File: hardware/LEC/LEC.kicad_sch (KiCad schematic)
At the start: 25 parts, among them J1 54-00278, J10 Conn_01x02_Socket, J11 Conn_01x02_Socket, J12 Conn_01x02_Socket, J13 Conn_01x02_Socket, J14 Conn_01x02_Socket, J15 Conn_01x02_Socket, J16 Conn_01x02_Socket, J17 Conn_01x03_Socket, J18 Conn_01x03_Socket, J19 Conn_01x03_Socket, J2 54-00278, J3 54-00278, J4 54-00278, J5 54-00278, J6 54-00278, J7 54-00278, J8 54-00278, J9 Conn_01x02_Socket, U1 Pico, U2 ZETA-433-SO, U3 ADS1243, U4 W25Q128JVSIQ

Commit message: Added LPFs and updated power circuits. Tidied up a bit
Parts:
- removed AE1: Antenna, symbol Device:Antenna
- removed J10, J11, J12, J13, J14, J15, J16, J9: Conn_01x02_Socket, symbol Connector:Conn_01x02_Socket
- removed J17, J18, J19: Conn_01x03_Socket, symbol Connector:Conn_01x03_Socket
- removed R1: 10K, symbol Device:R
- removed U2: ZETA-433-SO, symbol RF_AM_FM:ZETA-433-SO
- removed U3: ADS1243, Package_SO:TSSOP-20_4.4x6.5mm_P0.65mm, symbol Analog_ADC:ADS1243
- removed U4: W25Q128JVSIQ, SOIC_128JVSIQ_WIN, symbol W25q128JVSIQ:W25Q128JVSIQ
- added C1 (x2): 100n, Capacitor_SMD:C_1206_3216Metric, symbol Device:C
- added C14: 10u, symbol Device:C
- added D1: 1N5817, Diode_THT:D_DO-41_SOD81_P10.16mm_Horizontal, symbol Diode:1N5817
- added J10, J9: Conn_01x02, symbol Connector_Generic:Conn_01x02
- added J11, J12, J13, J9: 54-00278, TENSILITY_54-00278, symbol 4_Pin_M8_Socket_Female:54-00278
- added U15: MCP3564RT-E/ST, TSSOP20_ST_MCH, symbol MCP3564:MCP3564RT-E_ST
- added U2: LM2940CT-5.0/NOPB, T03B, symbol LM2940CT_5_0_NOPB:LM2940CT-5.0_NOPB
- added U3: MC7809CTG, TO-220AB_ONS, symbol MC7809CTG:MC7809CTG
- added U4: W25Q128JVSIQ, SOIC_128JVSIQ_WIN, symbol W25Q128JVSIQ:W25Q128JVSIQ
- added U5, U6: MAX31855KASA, Package_SO:SOIC-8_3.9x4.9mm_P1.27mm, symbol Sensor_Temperature:MAX31855KASA
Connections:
- net +12V: now also J10.1 (Pin_1), J11.3, J12.3, U2.1 (IN)
- net +3.3V: now also C1.1, C1.1, U5.4 (V_CC), U6.4 (V_CC)
- net GND: now also J10.2 (Pin_2), J11.2, J12.2
- net at J8.1: now also U6.3 (T+)
- net at J8.2: now also U6.2 (T-)
- net at U1.1 (GPIO0): now also J13.1
- net GPIO7: now reaches U1.10 (GPIO7)
- net GPIO7: now also U15.15 (SDI)
- net GPIO8: now reaches U1.11 (GPIO8)
- net GPIO8: now also U6.7 (SO)
- net GPIO9: now reaches U1.12 (GPIO9)
- net GPIO9: now also U6.6 (~{CS})
- net GNDD: now reaches U1.13 (GND)
- net GNDD: now also U1.18 (GND), U1.23 (GND), U1.28 (GND), U1.3 (GND), U1.38 (GND), U1.8 (GND), U15.19 (DGND), U2.2 (GND), U4.4 (GND)
- net GPIO10: now reaches U1.14 (GPIO10)
- net GPIO10: now also U6.5 (SCK)
- net GPIO12: now reaches U1.16 (GPIO12)
- net GPIO12: now also U5.7 (SO)
- net GPIO13: now reaches U1.17 (GPIO13)
- net GPIO13: now also U5.6 (~{CS})
- net GPIO14: now reaches U1.19 (GPIO14)
- net GPIO14: now also U5.5 (SCK)
- net at U1.2 (GPIO1): now also J13.2
- net GPIO16: now reaches U1.21 (GPIO16)
- net GPIO16: now also U4.2 (DO_(IO1))
- net GPIO17: now reaches U1.22 (GPIO17)
- net GPIO17: now also U4.1 (/CS)
- net GPIO18: now reaches U1.24 (GPIO18)
- net GPIO18: now also U4.6 (CLK)
- net GPIO19: now reaches U1.25 (GPIO19)
- net GPIO19: now also U4.5 (DI_(IO0))
- net at U1.27 (GPIO21): now also J12.1
- net at U1.29 (GPIO22): now also J11.1
- net ADC_Power_Circuit/SHDN: now reaches U1.31 (GPIO26_ADC0)
- net GNDA: now reaches U1.33 (AGND)
- net GNDA: now also J1.2, J2.2, J3.2, J4.2, J5.2, J6.2, J7.2, C1.2, C1.2, C14.1, J9.2 (Pin_2), U15.2 (AGND), U15.3 (REFIN-), U3.2 (GROUND), U5.1 (GND), U6.1 (GND)
- net at U1.36 (3V3): now also U4.8 (VCC)
- net at U1.39 (VSYS): now also D1.1 (K)
- net at U1.4 (GPIO2): now also J13.3
- net at U1.5 (GPIO3): now also J13.4
- net GPIO4: now reaches U1.6 (GPIO4)
- net GPIO4: now also U15.16 (SDO)
- net GPIO5: now reaches U1.7 (GPIO5)
- net GPIO5: now also U15.13 (*CS)
- net GPIO6: now reaches U1.9 (GPIO6)
- net GPIO6: now also U15.14 (SCK)
- net lowPassFilter2/V_{in}: now reaches J3.1
- net at J3.3: now also J1.3, J2.3, J4.3, J5.3, J6.3, J7.3, U3.3 (OUTPUT)
- net lowPassFilter4/V_{in}: now reaches J5.1
- net lowPassFilter6/V_{in}: now reaches J7.1
- net lowPassFilter/V_{in}: now reaches J1.1
- net lowPassFilter3/V_{in}: now reaches J4.1
- net lowPassFilter5/V_{in}: now reaches J6.1
- net lowPassFilter1/V_{in}: now reaches J2.1
- new net: D1.2 (A), U2.3 (OUT)
- new net: J9.1, U5.3 (T+)
- new net: J9.2, U5.2 (T-)
- new net ADC_Power_Circuit/AVDDOUT: U15.1 (AVDD)
- new net ADC_Power_Circuit/DVDDOUT: U15.20 (DVDD)
- new net ADC_Power_Circuit/REFIN+/OUT: C14.2, U15.4 (REFIN+/OUT)
- new net ADC_Power_Circuit/VIN: J9.1 (Pin_1), U3.1 (INPUT)
- new net lowPassFilter/V_{out}: U15.5 (CH0)
- new net lowPassFilter1/V_{out}: U15.6 (CH1)
- new net lowPassFilter2/V_{out}: U15.7 (CH2)
- new net lowPassFilter3/V_{out}: U15.8 (CH3)
- new net lowPassFilter4/V_{out}: U15.9 (CH4)
- new net lowPassFilter5/V_{out}: U15.10 (CH5)
- new net lowPassFilter6/V_{out}: U15.11 (CH6)
- no-connect marks 10 -> 29
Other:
- added sheet ADC_Power_Circuit (ADC_Power_Circuit.kicad_sch)
- added sheet lowPassFilter (lowPassFilter.kicad_sch)
- added sheet lowPassFilter1 (untitled.kicad_sch)
- added sheet lowPassFilter2 (untitled.kicad_sch)
- added sheet lowPassFilter3 (untitled.kicad_sch)
- added sheet lowPassFilter4 (untitled.kicad_sch)
- added sheet lowPassFilter5 (untitled.kicad_sch)
- added sheet lowPassFilter6 (untitled.kicad_sch)
- note added: "Pressure Transducer Connectors"
- note added: "RF Module SPI Connector"
- note added: "Sensor Power Connector (3S LiPo Battery, 11.1V)"
- note added: "Servomotor Power Connector (2S LiPo Battery, 7.4V)"
- note added: "Servomotor connectors"
- note added: "Thermocouple Connectors"
- moved on the sheet: J1, U1

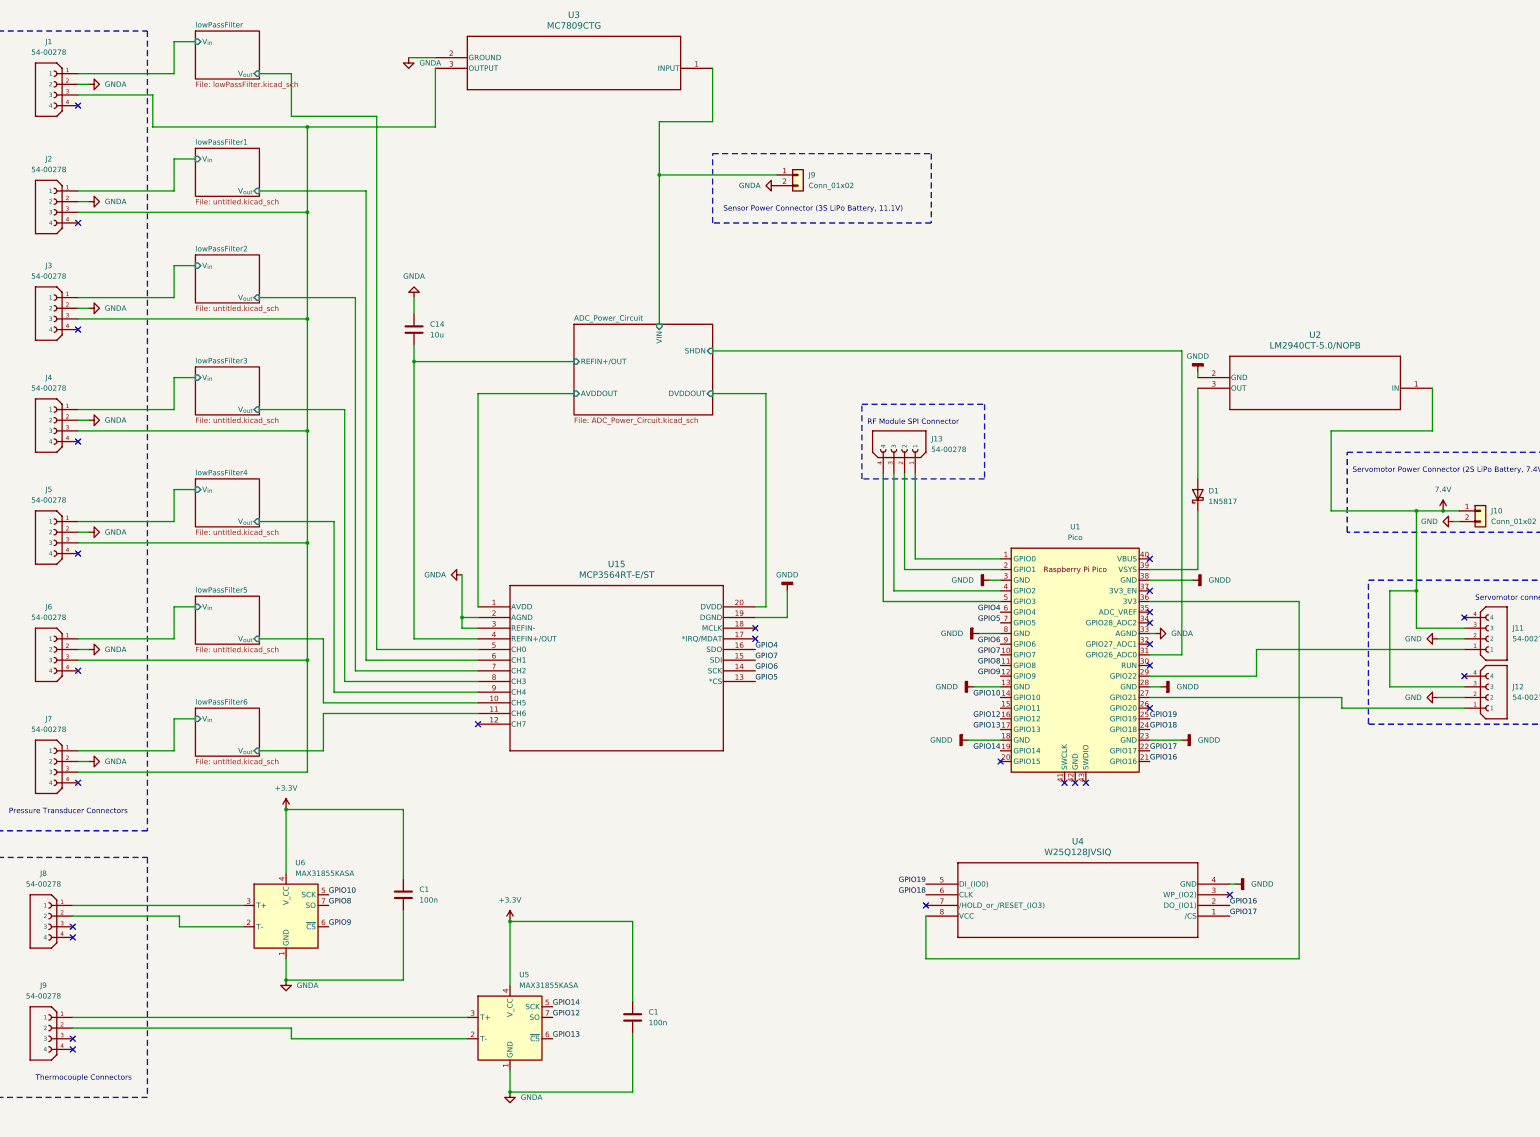
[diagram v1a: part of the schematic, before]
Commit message: Updated LVR selection and other optimizations. Need to update footprints and symbols
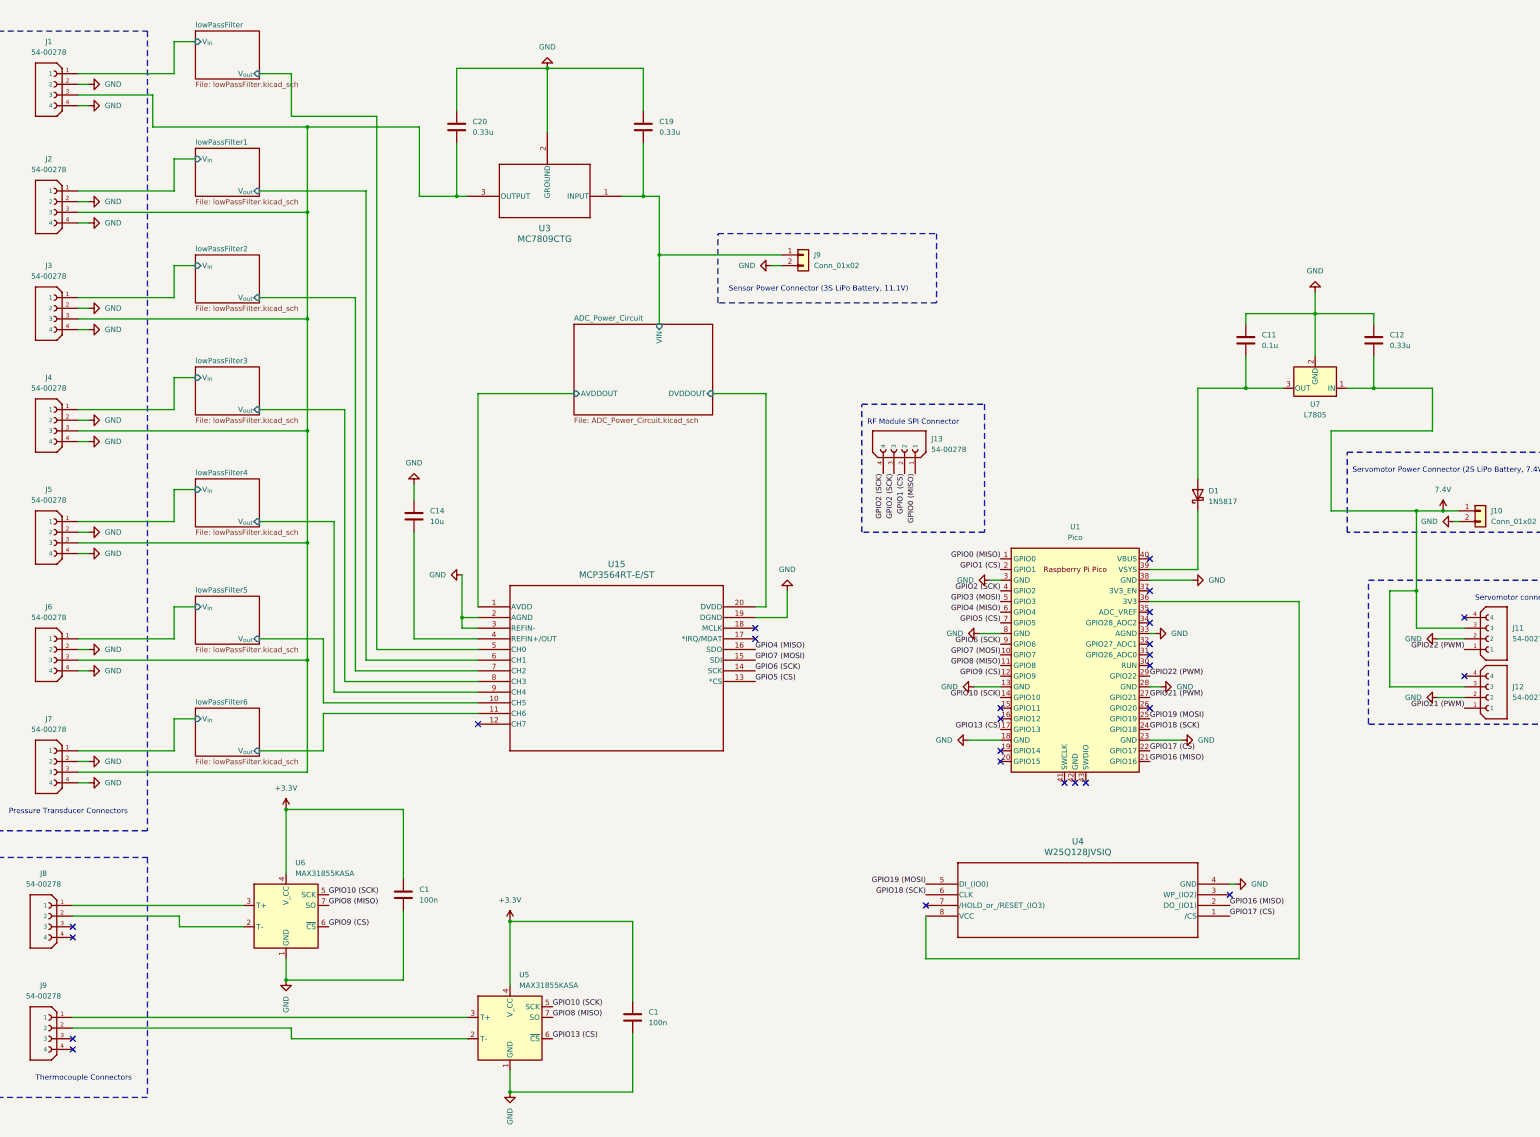
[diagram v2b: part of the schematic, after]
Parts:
- removed U2: LM2940CT-5.0/NOPB, T03B, symbol LM2940CT_5_0_NOPB:LM2940CT-5.0_NOPB
- added C11: 0.1u, symbol Device:C
- added C12, C19, C20: 0.33u, symbol Device:C
- added U7: L7805, symbol Regulator_Linear:L7805
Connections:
- net GNDA is gone; now on net GND: C1.2, C1.2, C14.1, J1.2, J2.2, J3.2, J4.2, J5.2, J6.2, J7.2, J9.2 (Pin_2), U1.33 (AGND), U15.2 (AGND), U15.3 (REFIN-), U3.2 (GROUND), U5.1 (GND), U6.1 (GND)
- net GNDD is gone; now on net GND: U1.13 (GND), U1.18 (GND), U1.23 (GND), U1.28 (GND), U1.3 (GND), U1.38 (GND), U1.8 (GND), U15.19 (DGND), U4.4 (GND)
- net +12V: now also C12.2, U7.1 (IN)
- net ADC_Power_Circuit/VIN: now also C19.2
- net GND: now also J1.4, J2.4, J3.4, J4.4, J5.4, J6.4, J7.4, C11.1, C12.1, C19.1, C20.1, U7.2 (GND)
- net at J1.3, J2.3, J3.3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: now also C20.2
- net GPIO0 (MISO): now reaches J13.1, U1.1 (GPIO0)
- net GPIO1 (CS): now reaches J13.2, U1.2 (GPIO1)
- net GPIO21 (PWM): now reaches J12.1, U1.27 (GPIO21)
- net GPIO22 (PWM): now reaches J11.1, U1.29 (GPIO22)
- net GPIO2 (SCK): now reaches J13.3, U1.4 (GPIO2)
- net GPIO2 (SCK): now also J13.4
- net GPIO3 (MOSI): now reaches U1.5 (GPIO3)
- net GPIO3 (MOSI): no longer J13.4
- net at D1.2 (A): now also C11.2, U7.3 (OUT)
- net ADC_Power_Circuit/REFIN+/OUT: no longer names the net of C14.2, U15.4 (REFIN+/OUT)
- net ADC_Power_Circuit/SHDN: no longer names the net of U1.31 (GPIO26_ADC0)
- net GPIO10 renamed GPIO10 (SCK)
- net GPIO10 (SCK): now also U5.5 (SCK)
- net GPIO12: no longer names the net of U1.16 (GPIO12)
- net GPIO12: no longer U5.7 (SO)
- net GPIO13 renamed GPIO13 (CS)
- net GPIO14: no longer names the net of U1.19 (GPIO14)
- net GPIO14: no longer U5.5 (SCK)
- net GPIO16 renamed GPIO16 (MISO)
- net GPIO17 renamed GPIO17 (CS)
- net GPIO18 renamed GPIO18 (SCK)
- net GPIO19 renamed GPIO19 (MOSI)
- net GPIO4 renamed GPIO4 (MISO)
- net GPIO5 renamed GPIO5 (CS)
- net GPIO6 renamed GPIO6 (SCK)
- net GPIO7 renamed GPIO7 (MOSI)
- net GPIO8 renamed GPIO8 (MISO)
- net GPIO8 (MISO): now also U5.7 (SO)
- net GPIO9 renamed GPIO9 (CS)
- no-connect marks 29 -> 26
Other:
- sheet ADC_Power_Circuit ports: added none; removed REFIN+/OUT, SHDN
- sheet lowPassFilter1: file untitled.kicad_sch -> lowPassFilter.kicad_sch
- sheet lowPassFilter2: file untitled.kicad_sch -> lowPassFilter.kicad_sch
- sheet lowPassFilter3: file untitled.kicad_sch -> lowPassFilter.kicad_sch
- sheet lowPassFilter4: file untitled.kicad_sch -> lowPassFilter.kicad_sch
- sheet lowPassFilter5: file untitled.kicad_sch -> lowPassFilter.kicad_sch
- sheet lowPassFilter6: file untitled.kicad_sch -> lowPassFilter.kicad_sch
- moved on the sheet: C14, J9, U3

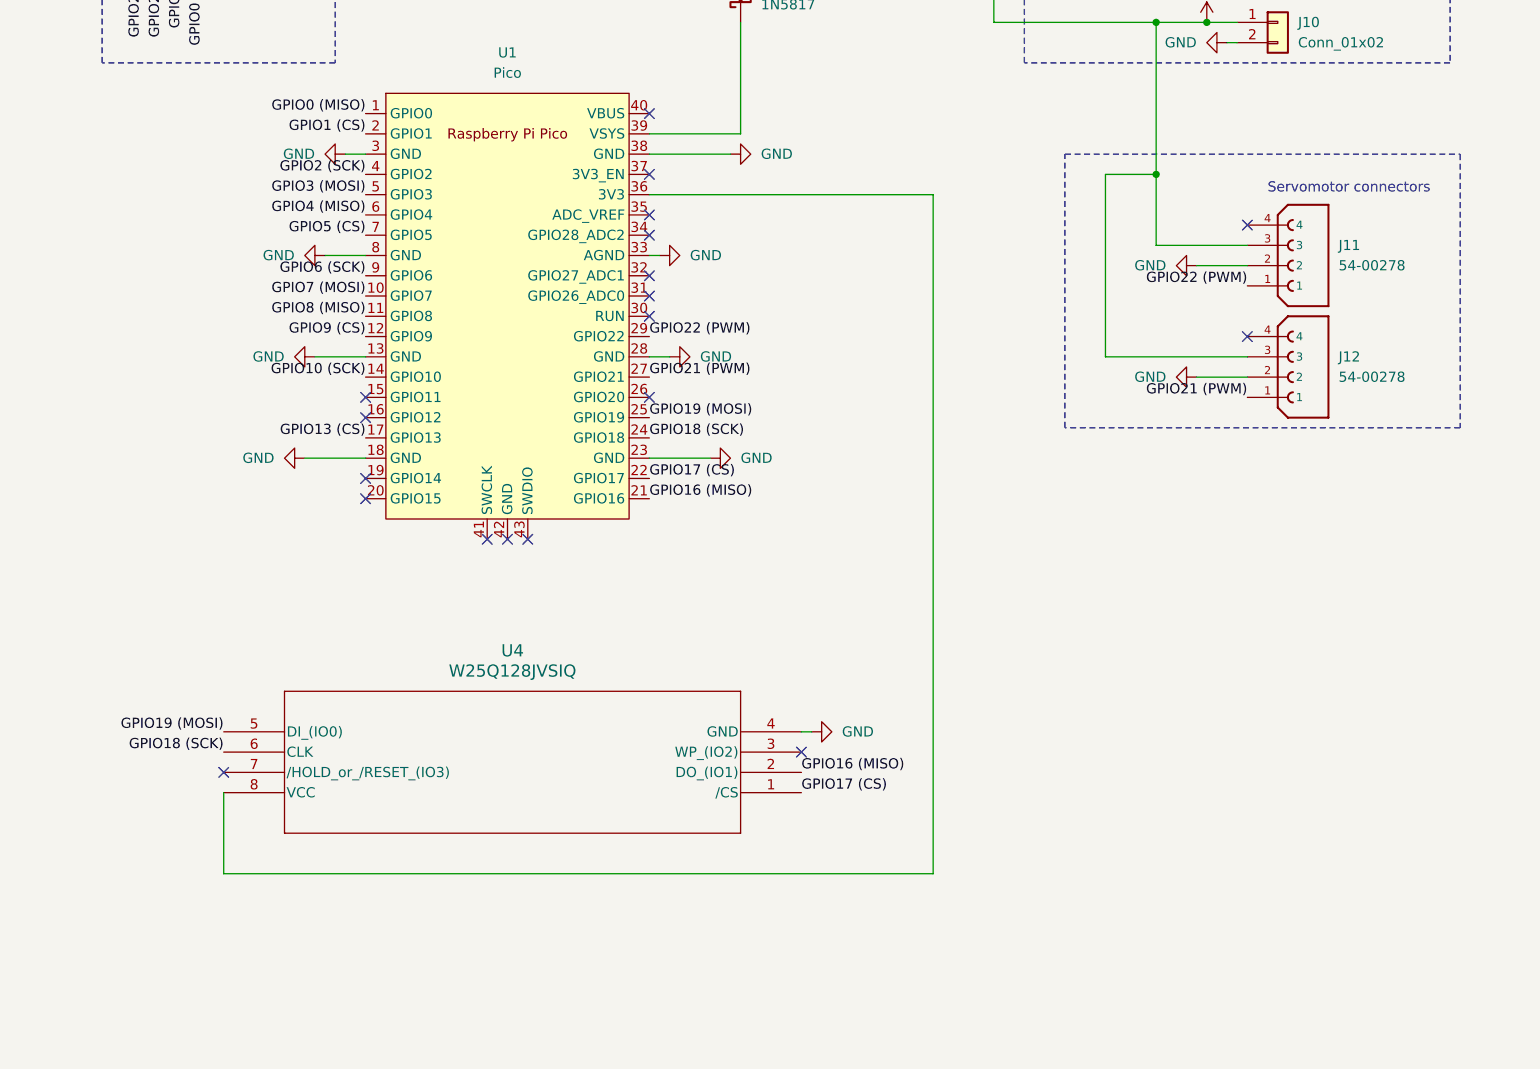
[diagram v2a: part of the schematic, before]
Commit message: Updated wiring of flash chip, connected 3V3 net, and added PWM pulldowns
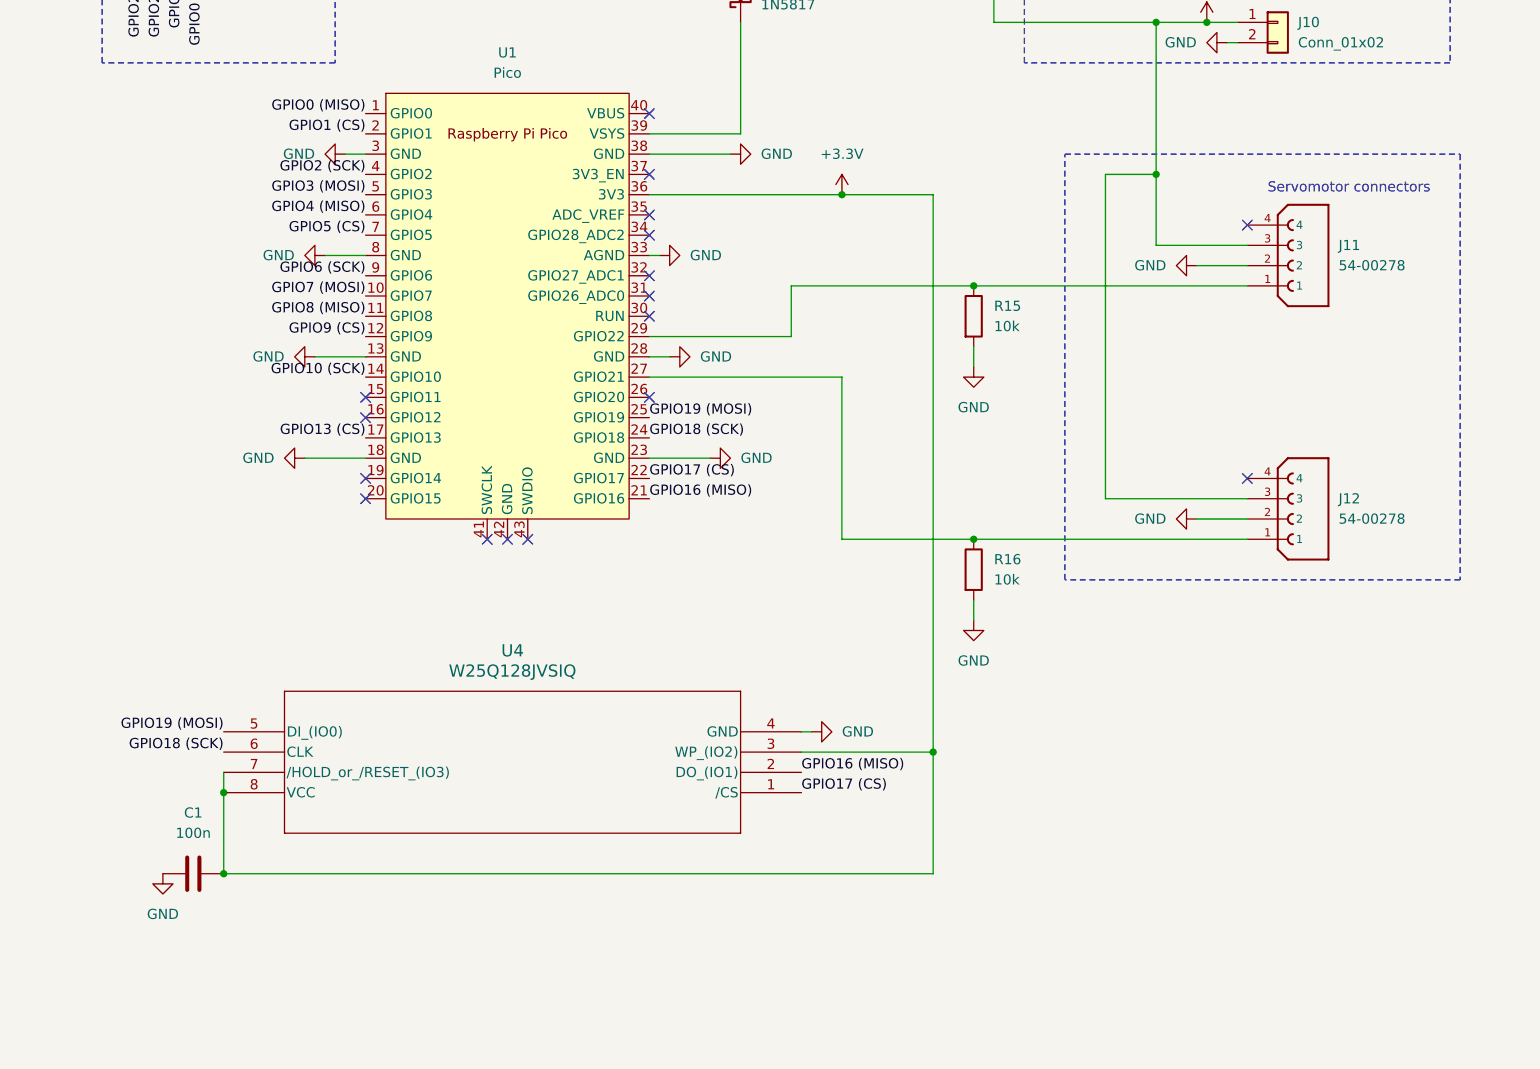
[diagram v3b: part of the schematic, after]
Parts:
- added C1: 100n, Capacitor_SMD:C_1206_3216Metric, symbol Device:C
- added R15, R16: 10k, symbol Device:R
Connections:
- net +3.3V: now also U1.36 (3V3), U4.3 (WP_(IO2)), U4.7 (/HOLD_or_/RESET_(IO3)), U4.8 (VCC), C1.2
- net GND: now also C1.1, R15.2, R16.2
- net GPIO21 (PWM): no longer names the net of J12.1, U1.27 (GPIO21)
- net GPIO21 (PWM): now also R16.1
- net GPIO22 (PWM): no longer names the net of J11.1, U1.29 (GPIO22)
- net GPIO22 (PWM): now also R15.1
- no-connect marks 26 -> 24
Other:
- moved on the sheet: J12
